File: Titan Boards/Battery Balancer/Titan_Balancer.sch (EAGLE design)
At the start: 83 parts, among them IC1 REG1117, IC2 SN74LV11AD, P1 39-30-04, P2 39-30-10, P4 39-30-04, P5 39-30-06, Q1 SPD30P06PTO252, Q12 310mA/60V/1.6Ω, Q2 SPB80P06P, Q3 SPB80P06P, Q4 SPD30P06PTO252, Q5 MOSFET-NCH-AO3404A, Q9 MOSFET-NCH-AO3404A, U1 I6A4W020A033V-001-R, U2 I6A4W020A033V-001-R

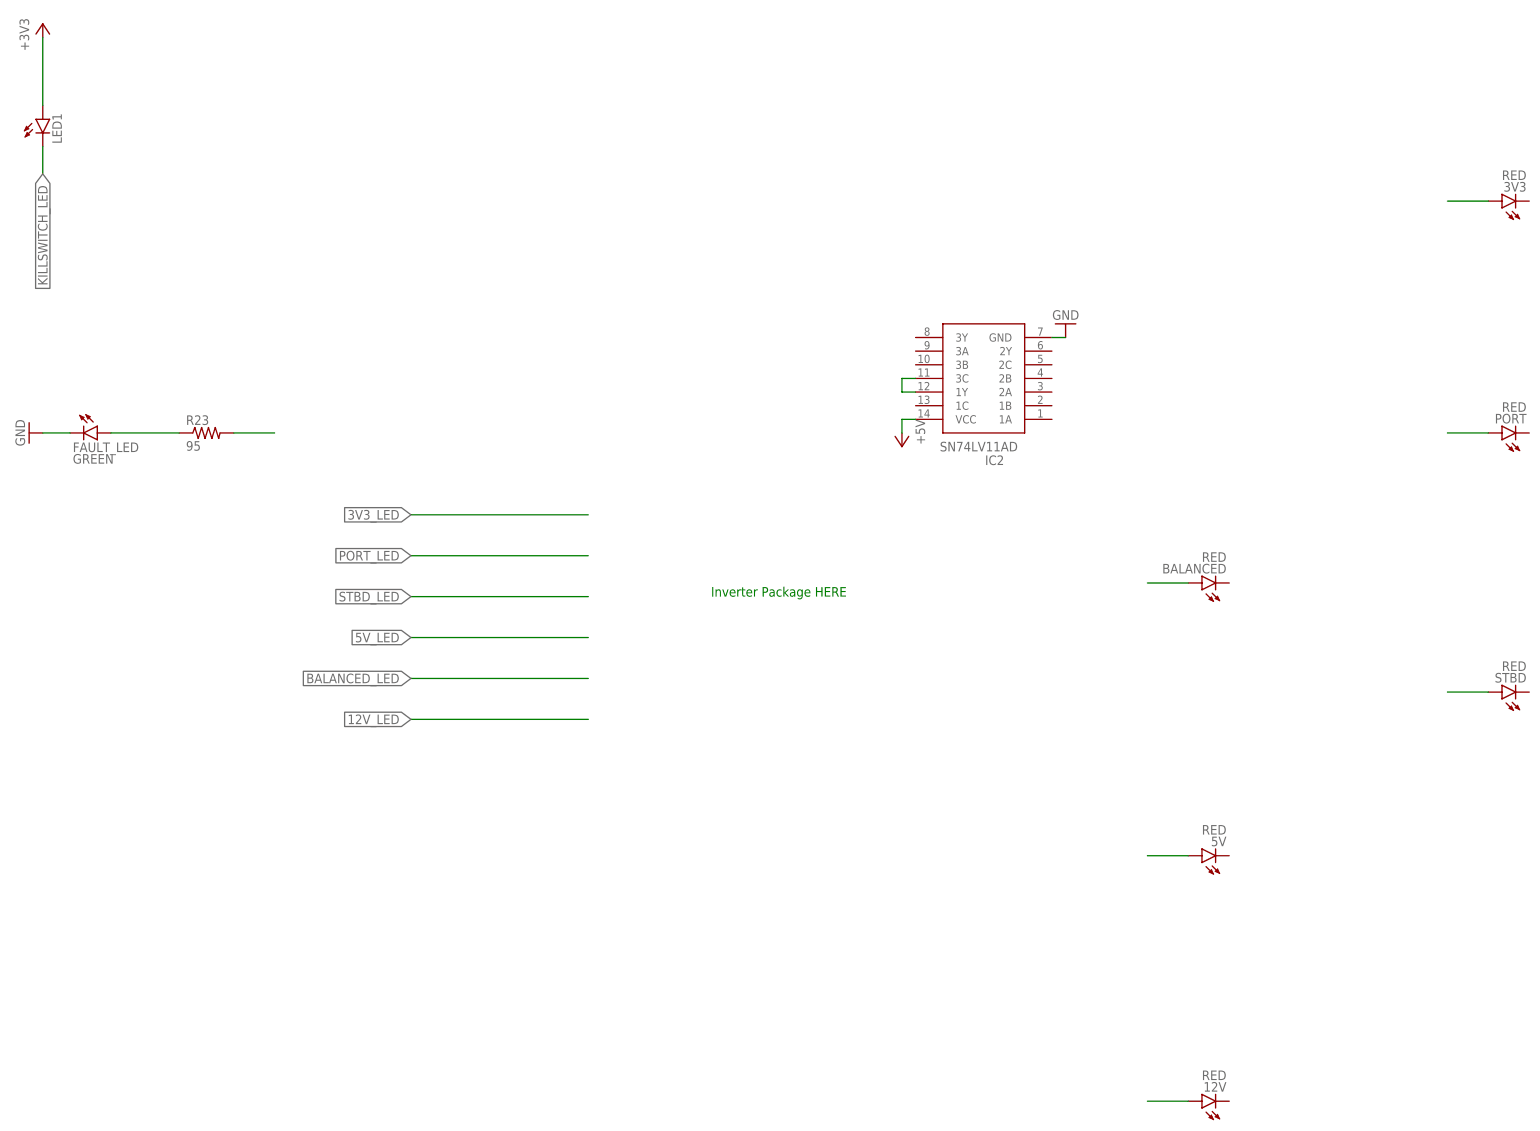
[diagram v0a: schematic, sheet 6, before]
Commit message: put led's to and gate, voltage needs stepped up or down
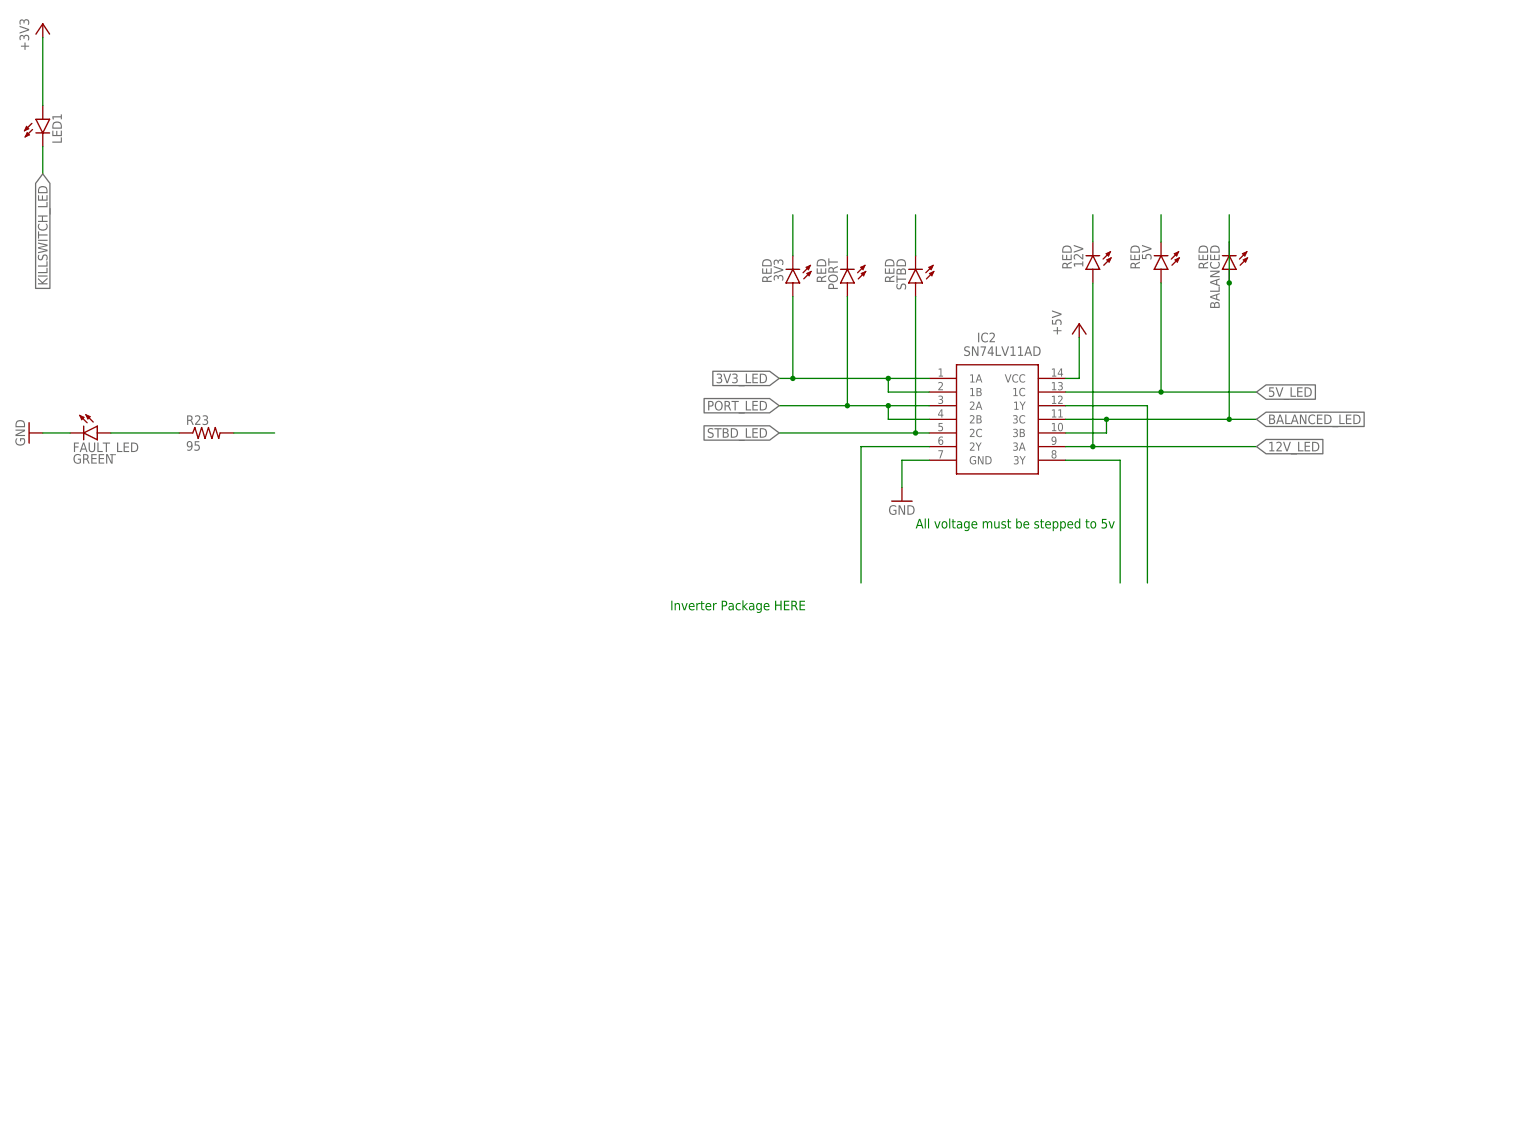
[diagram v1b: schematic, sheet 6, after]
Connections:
- new net N$31: 5V.C
- net 12V_LED: now also 12V.A, IC2.3A
- net 3V3_LED: now also 3V3.A, IC2.1A, IC2.1B
- net 5V_LED: now also 5V.A, IC2.1C
- net BALANCED_LED: now also BALANCED.A, BALANCED.C, IC2.3B, IC2.3C
- net N$20: now also 3V3.C; no longer 5V.A
- net N$26: now also IC2.3Y; no longer BALANCED.A
- net N$27: now also IC2.2Y; no longer STBD.A
- net N$28: now also PORT.C; no longer PORT.A
- net N$29: now also STBD.C; no longer 3V3.A
- net N$30: now also 12V.C; no longer IC2.1Y, IC2.3C
- net N$9: now also IC2.1Y; no longer 12V.A
- net PORT_LED: now also IC2.2A, IC2.2B, PORT.A
- net STBD_LED: now also IC2.2C, STBD.A
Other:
- note added: "All voltage must be stepped to 5v"
- moved on the sheet: 12V, 3V3, 5V, BALANCED, IC2, PORT, STBD

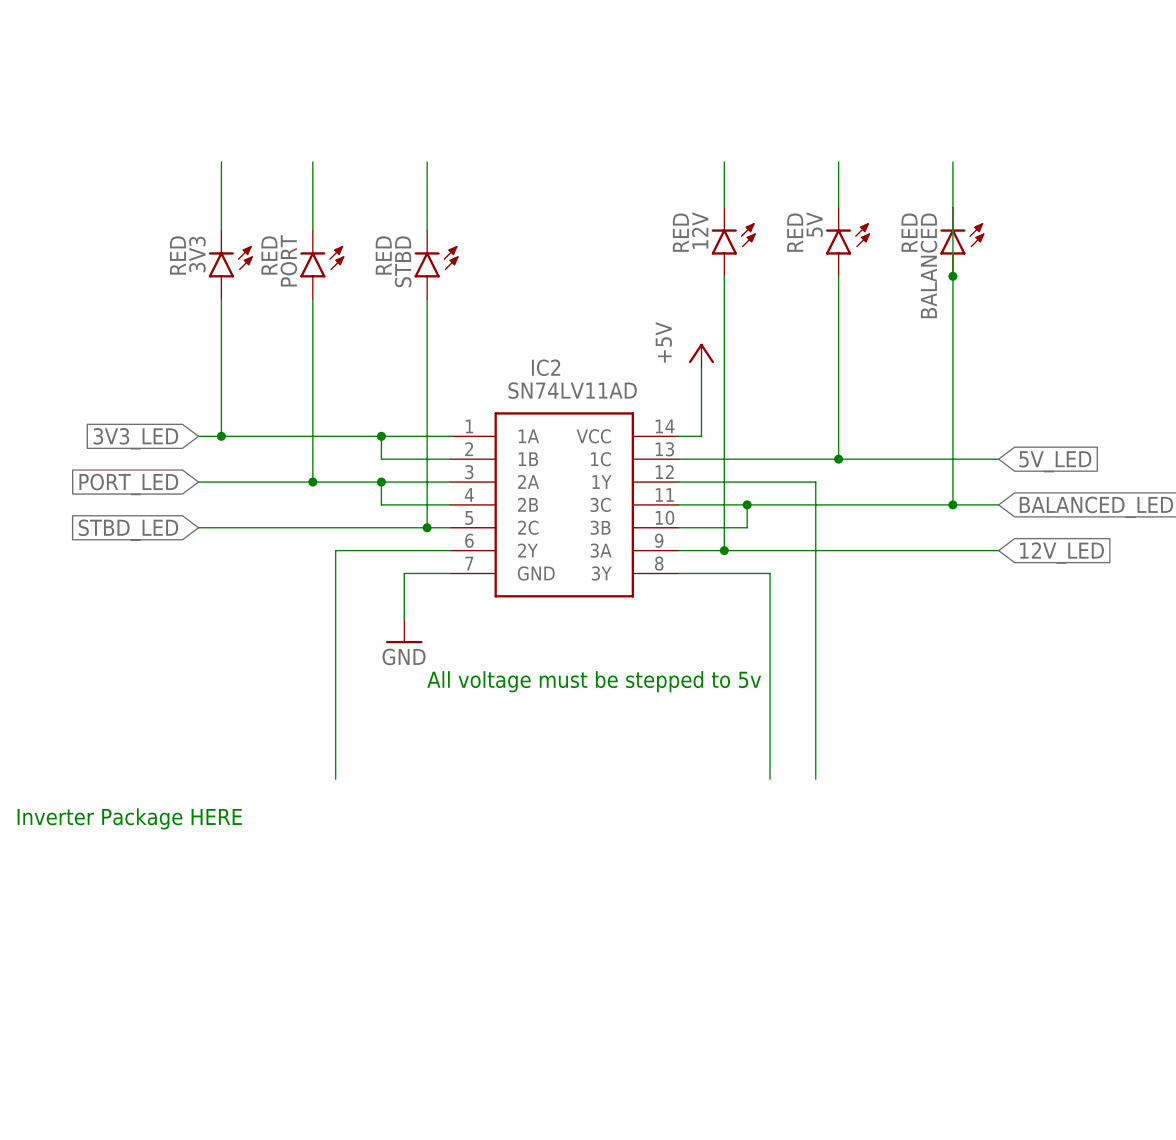
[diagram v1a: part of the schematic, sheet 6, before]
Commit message: Organized Board Some more, redid some pin organization for later
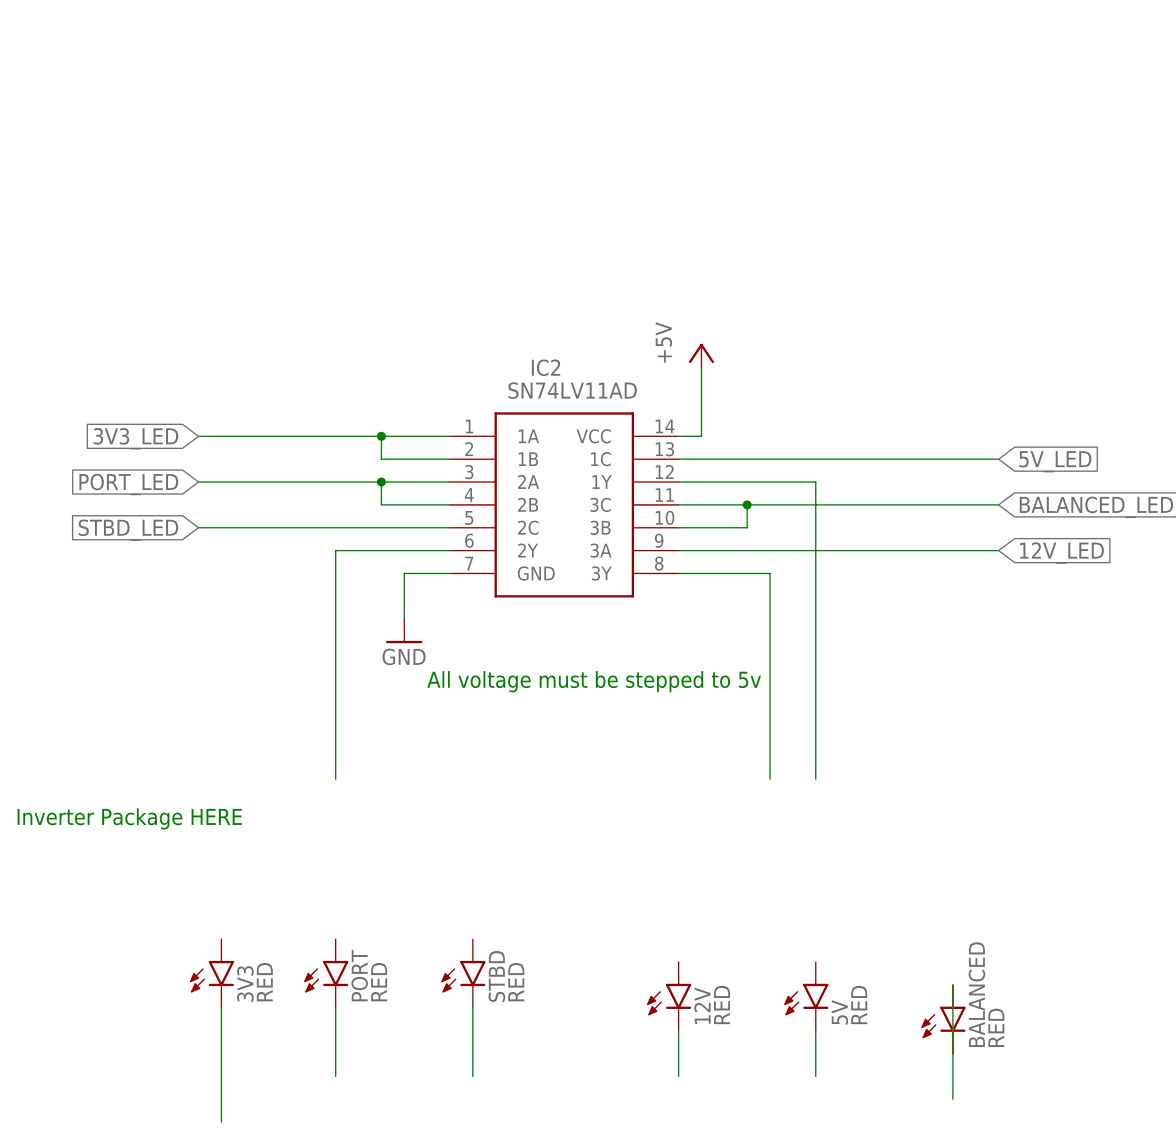
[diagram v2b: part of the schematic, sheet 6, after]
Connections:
- new net N$32: BALANCED.A, BALANCED.C
- net +12V: now also P2.10, P2.6, P2.7, P2.8, P2.9, P4.3, P4.4, P5.5, P5.6; no longer P2.1, P2.2, P2.3, P2.4, P2.5, P4.1, P4.2, P5.2, P5.3
- net +5V: now also P1.3, P1.4; no longer P1.1, P1.2
- net 12V_LED: no longer 12V.A
- net 3V3_LED: no longer 3V3.A
- net 5V_LED: no longer 5V.A
- net BALANCED_LED: no longer BALANCED.A, BALANCED.C
- net GND: now also BATTERYCONNECTOR.1, BATTERYCONNECTOR.2, BATTERYCONNECTOR.3, BATTERYCONNECTOR.4, BATTERYCONNECTOR.5, BATTERYCONNECTOR.6, BATTERYCONNECTOR.7, BATTERYCONNECTOR.8, P1.1, P1.2, P2.1, P2.2, P2.3, P2.4, P4.1, P4.2, P5.2, P5.3; no longer BATTERYCONNECTOR.10, BATTERYCONNECTOR.11, BATTERYCONNECTOR.12, BATTERYCONNECTOR.13, BATTERYCONNECTOR.14, BATTERYCONNECTOR.15, BATTERYCONNECTOR.16, BATTERYCONNECTOR.9, P1.3, P1.4, P2.6, P2.7, P2.8, P2.9, P4.3, P4.4, P5.5, P5.6
- net PORT_BAT: now also BATTERYCONNECTOR.13, BATTERYCONNECTOR.14, BATTERYCONNECTOR.15, BATTERYCONNECTOR.16; no longer BATTERYCONNECTOR.5, BATTERYCONNECTOR.6, BATTERYCONNECTOR.7, BATTERYCONNECTOR.8
- net PORT_LED: no longer PORT.A
- net STBD_BAT: now also BATTERYCONNECTOR.10, BATTERYCONNECTOR.11, BATTERYCONNECTOR.12, BATTERYCONNECTOR.9; no longer BATTERYCONNECTOR.1, BATTERYCONNECTOR.2, BATTERYCONNECTOR.3, BATTERYCONNECTOR.4
- net STBD_LED: no longer STBD.A
- net XAVIER_ALT: now also P2.5; no longer P2.10
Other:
- moved on the sheet: 12V, 3V3, 5V, BALANCED, PORT, STBD

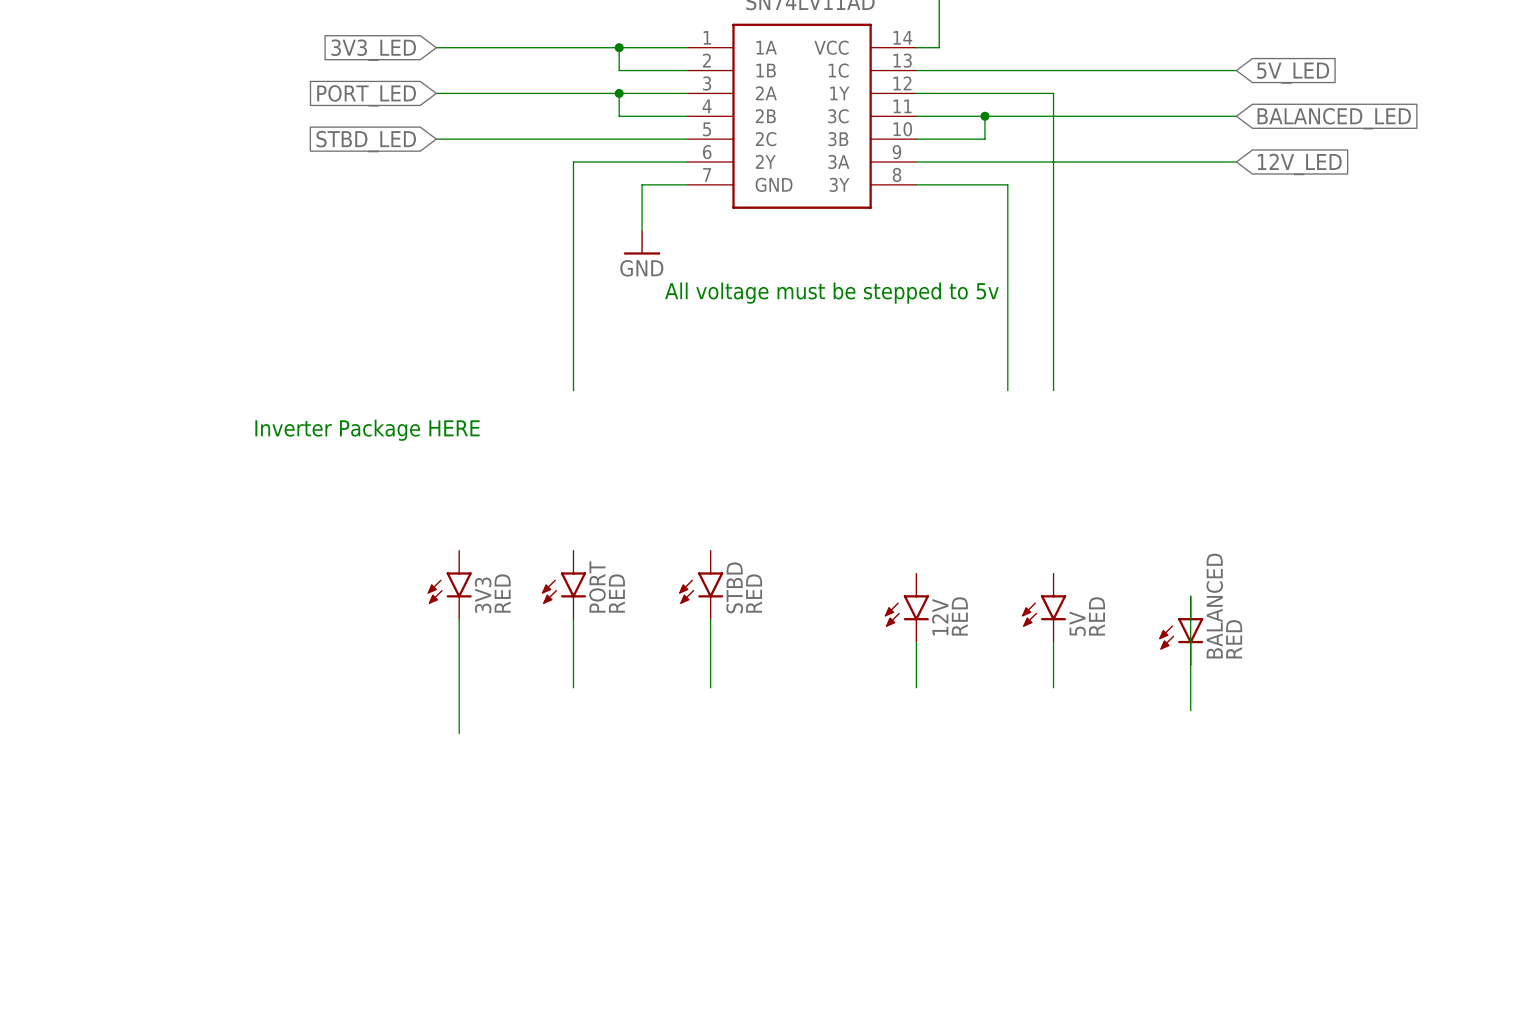
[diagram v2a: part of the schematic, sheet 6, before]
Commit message: Uhh added Iverter library and set up leds for pins, still needs step up thing for leds
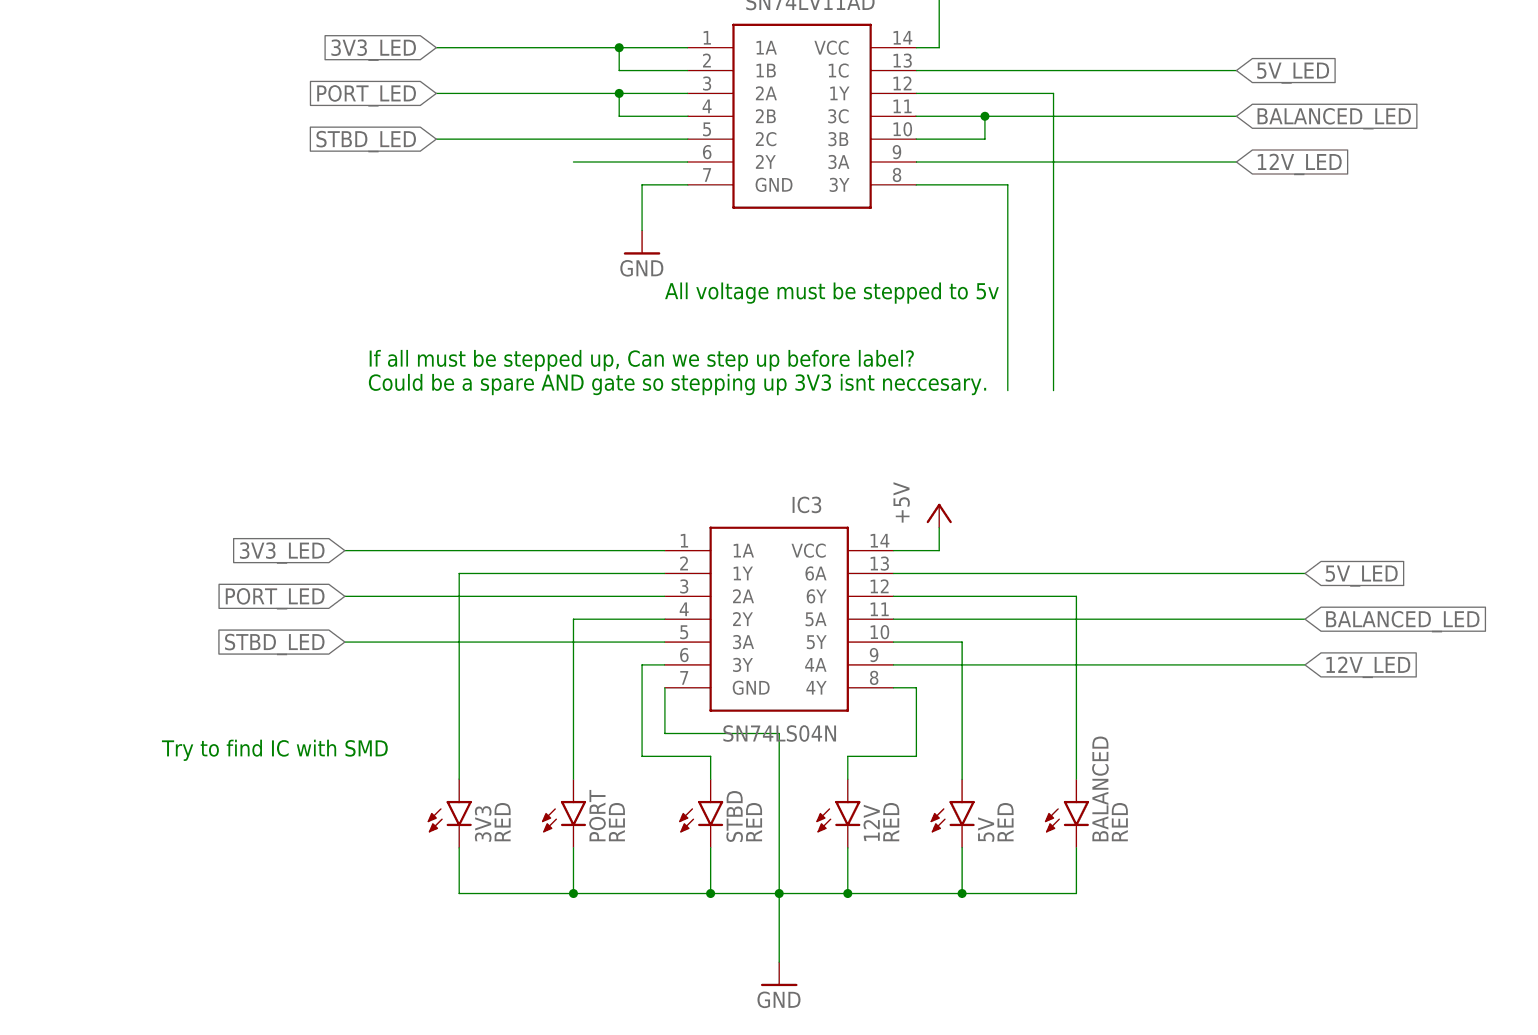
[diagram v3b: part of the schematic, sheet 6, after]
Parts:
- added IC3: SN74LS04N, SN74LS04N:SN74LS04N
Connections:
- net +5V: now also IC3.VCC
- net 12V_LED: now also IC3.4A
- net 3V3_LED: now also IC3.1A
- net 5V_LED: now also IC3.6A
- net BALANCED_LED: now also IC3.5A
- net GND: now also 12V.C, 3V3.C, 5V.C, BALANCED.C, IC3.GND, PORT.C, STBD.C
- net N$20: now also 3V3.A, IC3.1Y; no longer 3V3.C
- net N$28: now also IC3.2Y, PORT.A; no longer PORT.C
- net N$29: now also IC3.3Y, STBD.A; no longer STBD.C
- net N$30: now also 12V.A, IC3.4Y; no longer 12V.C
- net N$31: now also 5V.A, IC3.5Y; no longer 5V.C
- net N$32: now also IC3.6Y; no longer BALANCED.C
- net PORT_LED: now also IC3.2A
- net STBD_LED: now also IC3.3A
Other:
- note added: "If all must be stepped up, Can we step up before label? Could be a spare AND gate so stepping up 3V3 isnt neccesary."
- note added: "Try to find IC with SMD"
- note removed: "Inverter Package HERE"
- note removed: "Mobo computer and jetson have been combined to form Xavier computer"
- moved on the sheet: 12V, 3V3, 5V, BALANCED, PORT, STBD
